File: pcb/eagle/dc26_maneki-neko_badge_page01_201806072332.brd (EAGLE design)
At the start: 100 x 80 mm, 49 parts, among them IC1 STM32F030C8T, T1 RK7002BMT116, U2 ESP01, X1 22-23-2021, X2 22-23-2031

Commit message: board outline in, some minor edits to schematic, board ready for component placement
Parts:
- removed LED1, LED2: WS2812B5050, adafruit_2015:WS2812B
- removed U$1, U$2: (no value), PSA08-11SRWA:PSA08-11SRWA
- removed U$5: PAM2301CAAB330, PAM2301CAAB120:SOT95P280X100-5N
- added C10: 1uF/16V/X7R, rcl:C0805
- added D1, D2: (no value), PSA08-11SRWA:PSA08-11SRWA
- added H3: TSW-102-07-G-D, con-samtec:TSW-102-XX-G-D
- added R26, R27, R28: 10k/5%, rcl:R0805
- added R29: NO POP, rcl:R0805
- added U3: ESP01, esp8266modules:ESP01
- C1: value SHORT -> 10uF/16V/X5R
- C3: value 10uF/16V/X5R -> SHORT
- R25: value 10k/5% -> 1k/5%
- U2: value ESP01 -> PAM2301CAAB330; device esp8266modules:ESP01 -> PAM2301CAAB120:SOT95P280X100-5N
- U5, U6: value (none) -> MIC2005A-1YM5-TR
- moved R3 129.2 mm to (38.5, 47.3), turned to 180 degrees
- moved C1 124.9 mm to (42.8, 43.6)
- moved C3 114.4 mm to (38.6, 39.1)
- moved C2 110.8 mm to (34.3, 44.8)
- moved R1 100.5 mm to (38.6, 41.2), turned to 180 degrees
- moved L1 95.7 mm to (35.7, 42.2), turned to 180 degrees
- moved U2 67.8 mm to (38.5, 44.1)
- moved R12 12.7 mm to (-105.4, -106.7)
- moved R14 12.7 mm to (-118.1, -106.7)
- moved R15 12.7 mm to (-105.4, -113.0)
- moved R17 12.7 mm to (-118.1, -113.0)
- moved R18 6.35 mm to (-111.8, -119.4)
- moved R19 6.35 mm to (-118.1, -119.4)
- renumbered IC1 to U1, U$13 to H1, U$3 to U6, U$4 to U5, U$6 to U4, X2 to H2
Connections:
- removed net VCC: C4.1, C5.1, C6.1, H1.1, R21.2, R22.2, U5.1, U6.1
- removed net VDDA: U1.9
- removed net VSSA: U1.8
- new net BOOT0: R28.2, R29.1, U1.44
- new net I2C1_SCL: H3.4, R26.1, U1.35
- new net I2C1_SDA: H3.3, R27.1, U1.36
- net !RESET: now also U1.7
- net 3V3: now also C10.1, C2.1, C4.1, C5.1, C6.1, H1.1, H3.1, R21.2, R22.2, R26.2, R27.2, R29.2, U1.9, U5.1, U6.1; no longer C1.1
- net ESP-CH_PD: now also U3.CH_PD; no longer U2.CH_PD
- net ESP-GPIO0: now also U3.GPIO0; no longer U2.GPIO0
- net ESP-GPIO2: now also U3.GPIO2; no longer U2.GPIO2
- net ESP-RST: now also U3.RST; no longer U2.RST
- net ESP-RXD: now also U3.RX; no longer U2.RX
- net ESP-TXD: now also U3.TX; no longer U2.TX
- net GND: now also C1.2, C10.2, H3.2, R28.1, U1.8, U2.2, U3.GND; no longer C3.2, LED1.3-GND, LED2.3-GND, U$5.2, U2.GND
- net LED-ANODE-LEFT: now also D1.11; no longer U$1.11
- net LED-ANODE-RIGHT: now also D2.11; no longer U$2.11
- net LED-SEG-A: now also D1.1, D2.1, R18.2; no longer R19.2, U$1.1, U$2.1
- net LED-SEG-B: now also D1.18, D2.18, R19.2; no longer R18.2, U$1.18, U$2.18
- net LED-SEG-C: now also D1.16, D2.16, R15.2; no longer R17.2, U$1.16, U$2.16
- net LED-SEG-D: now also D1.13, D2.13; no longer U$1.13, U$2.13
- net LED-SEG-DP: now also D1.12, D2.12; no longer U$1.12, U$2.12
- net LED-SEG-E: now also D1.10, D2.10, R17.2; no longer R15.2, U$1.10, U$2.10
- net LED-SEG-F: now also D1.9, D2.9, R12.2; no longer R14.2, U$1.9, U$2.9
- net LED-SEG-G: now also D1.8, D2.8; no longer U$1.8, U$2.8
- net LED-SEG-H: now also D1.4, D2.4, R14.2; no longer R12.2, U$1.4, U$2.4
- net LED-SEG-K: now also D1.3, D2.3; no longer U$1.3, U$2.3
- net LED-SEG-M: now also D1.2, D2.2; no longer U$1.2, U$2.2
- net LED-SEG-N: now also D1.17, D2.17; no longer U$1.17, U$2.17
- net LED-SEG-P: now also D1.15, D2.15; no longer U$1.15, U$2.15
- net LED-SEG-R: now also D1.14, D2.14; no longer U$1.14, U$2.14
- net LED-SEG-S: now also D1.6, D2.6; no longer U$1.6, U$2.6
- net LED-SEG-T: now also D1.7, D2.7; no longer U$1.7, U$2.7
- net LED-SEG-U: now also D1.5, D2.5; no longer U$1.5, U$2.5
- net N$1: now also U2.3; no longer U$5.3
- net N$2: now also U2.1; no longer U$5.1
- net N$3: now also C3.2, U2.5; no longer C1.2, U$5.5
- net PB0: now also R18.1; no longer R19.1
- net PB1: now also R19.1; no longer R18.1
- net PB2: now also R15.1; no longer R17.1
- net PB4: now also R17.1; no longer R15.1
- net PB5: now also R12.1; no longer R14.1
- net PB7: now also R14.1; no longer R12.1
- net VBAT: now also C1.1, U2.4; no longer C2.1, U$5.4
- net VDD: no longer LED1.1-VDD, LED2.1-VDD
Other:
- board size 100 x 80 mm -> 75.8 x 126.7 mm

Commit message: some component placement, eyes locked in
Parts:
- moved R29 433.2 mm to (61.4, 23.4), flipped to the bottom, turned to 90 degrees
- moved R28 424.5 mm to (55.2, 23.4), flipped to the bottom, turned to 90 degrees
- moved C10 415.8 mm to (49.1, 23.4), flipped to the bottom, turned to 90 degrees
- moved R27 407.1 mm to (42.9, 23.4), flipped to the bottom, turned to 90 degrees
- moved R26 398.4 mm to (36.8, 23.4), flipped to the bottom, turned to 90 degrees
- moved C9 389.8 mm to (30.6, 23.4), flipped to the bottom, turned to 90 degrees
- moved R22 386.3 mm to (55.4, 42.1), flipped to the bottom
- moved R20 385.1 mm to (52.5, 102.3), flipped to the bottom, turned to 270 degrees
- moved R21 384.0 mm to (55.4, 44.4), flipped to the bottom
- moved C8 382.6 mm to (59.6, 41.9), flipped to the bottom
- moved R25 381.1 mm to (24.5, 23.4), flipped to the bottom, turned to 90 degrees
- moved U4 380.3 mm to (60.2, 45.3), flipped to the bottom
- moved H2 378.0 mm to (54.5, 17.5), flipped to the bottom
- moved R23 378.0 mm to (46.4, 34.3), flipped to the bottom
- moved R24 378.0 mm to (46.4, 28.1), flipped to the bottom
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
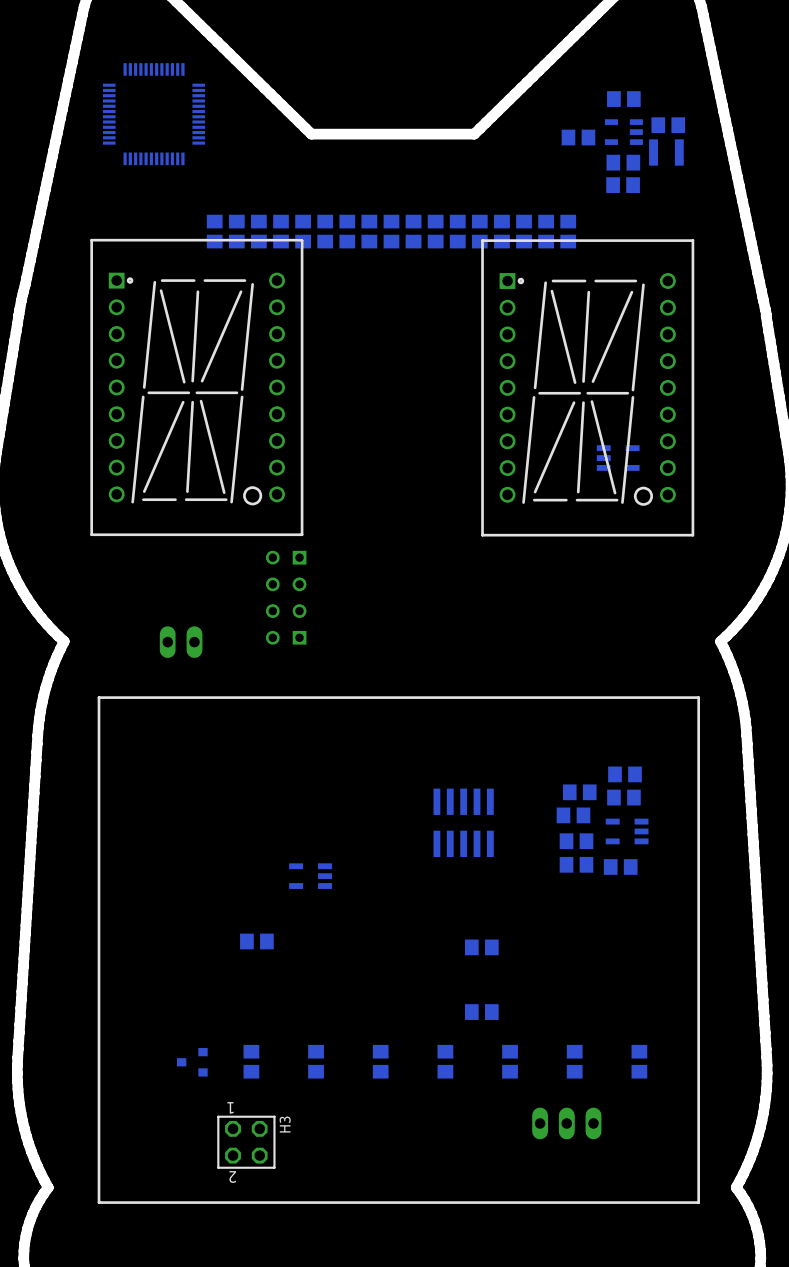
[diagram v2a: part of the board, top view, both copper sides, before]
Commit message: more layout. changed out connectors to support a clean 'art' (top) side. shooting for 2 layers, might need to be 4 to avoid a ton of routing time.
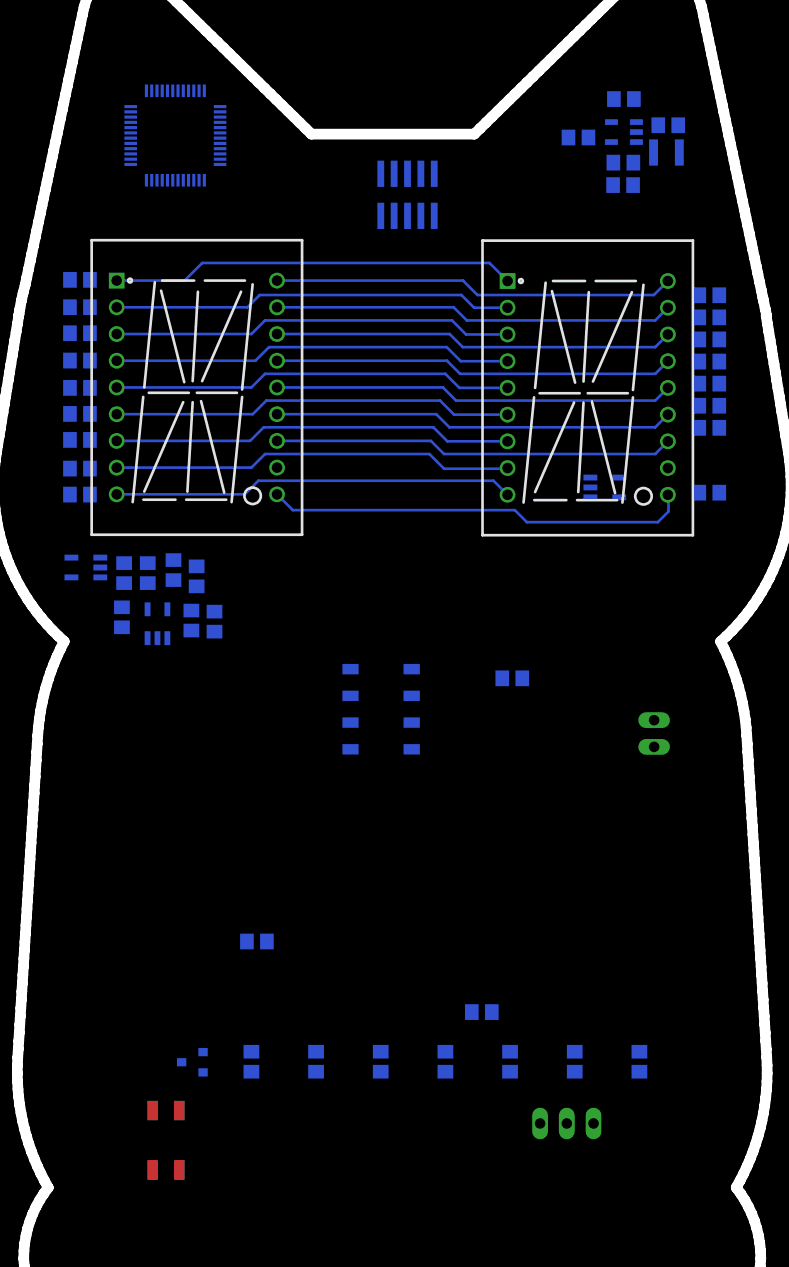
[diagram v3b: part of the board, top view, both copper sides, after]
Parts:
- H3: value TSW-102-07-G-D -> SHITTY-ADDON-HEADER-MASTER; device con-samtec:TSW-102-XX-G-D -> dc26-shitty-addon:2X2-0.1INCH-FEMALE-SMT
- U3: value ESP01 -> NPTC042KFMS-RC; device esp8266modules:ESP01 -> NPTC042KFMS-RC:NPTC042KFMS-RC
- moved H1 59.9 mm to (41.9, 103.8)
- moved C8 53.0 mm to (12.2, 65.6), turned to 90 degrees
- moved R22 51.2 mm to (12.4, 69.8), turned to 90 degrees
- moved U4 48.8 mm to (15.6, 65.0), turned to 90 degrees
- moved R21 48.1 mm to (14.6, 69.8), turned to 90 degrees
- moved X1 45.8 mm to (62.8, 54.6), turned to 90 degrees
- moved C7 44.6 mm to (17.1, 70.1), turned to 90 degrees
- moved C6 44.4 mm to (18.8, 65.3), turned to 90 degrees
- moved C5 41.8 mm to (19.3, 69.5), turned to 90 degrees
- moved C4 41.6 mm to (21.0, 65.2), turned to 90 degrees
- moved R12 38.8 mm to (8.19, 77.3), turned to 180 degrees
- moved U6 36.3 mm to (8.75, 70.4)
- moved R13 35.6 mm to (8.19, 79.8), turned to 180 degrees
- moved R5 32.2 mm to (8.19, 82.5), turned to 180 degrees
- moved R6 29.0 mm to (8.19, 85.0), turned to 180 degrees
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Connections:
- net 3V3: now also H3.VCC; no longer H3.1
- net ESP-CH_PD: now also U3.3; no longer U3.CH_PD
- net ESP-GPIO0: now also U3.6; no longer U3.GPIO0
- net ESP-GPIO2: now also U3.4; no longer U3.GPIO2
- net ESP-RST: now also U3.5; no longer U3.RST
- net ESP-RXD: now also U3.8; no longer U3.RX
- net ESP-TXD: now also U3.1; no longer U3.TX
- net ESP-VCC: now also U3.7
- net GND: now also H3.GND, U3.2; no longer H3.2, U3.GND
- net I2C1_SCL: now also H3.SCL; no longer H3.4
- net I2C1_SDA: now also H3.SDA; no longer H3.3
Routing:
- net LED-SEG-E: track 0.00 -> 40.3 mm
- net LED-SEG-A: track 0.00 -> 38.6 mm
- net LED-SEG-G: track 0.00 -> 38.3 mm
- net LED-SEG-B: track 0.00 -> 38.3 mm
- net LED-SEG-S: track 0.00 -> 38.2 mm
- net LED-SEG-H: track 0.00 -> 38.2 mm
- net LED-SEG-F: track 0.00 -> 38.2 mm
- net LED-SEG-U: track 0.00 -> 38.2 mm
- net LED-SEG-T: track 0.00 -> 38.2 mm
- net LED-SEG-K: track 0.00 -> 38.2 mm
- net LED-SEG-P: track 0.00 -> 38.2 mm
- net LED-SEG-N: track 0.00 -> 38.2 mm
- net LED-SEG-D: track 0.00 -> 38.2 mm
- net LED-SEG-C: track 0.00 -> 38.2 mm
- net LED-SEG-R: track 0.00 -> 38.2 mm
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
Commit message: completely regretting my decision to use eagle
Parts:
- added C11, C12: 1uF/16V/X7R, rcl:C0805
- moved R29 91.6 mm to (30.4, 109.6), turned to 180 degrees
- moved R28 87.6 mm to (30.3, 107.4), turned to 0 degrees
- moved C10 85.1 mm to (17.3, 102.4), turned to 180 degrees
- moved C2 75.4 mm to (15.3, 55.0), turned to 180 degrees
- moved R3 74.3 mm to (19.5, 52.5), turned to 0 degrees
- moved L1 69.6 mm to (16.7, 57.6), turned to 0 degrees
- moved U2 69.1 mm to (19.5, 55.6), turned to 180 degrees
- moved H2 67.1 mm to (10.8, 68.4), turned to 270 degrees
- moved R1 64.5 mm to (19.5, 58.5), turned to 0 degrees
- moved C1 63.6 mm to (23.8, 56.1), turned to 180 degrees
- moved C3 61.2 mm to (19.6, 60.7), turned to 180 degrees
- moved R27 46.4 mm to (9.27, 55.3)
- moved T1 45.6 mm to (16.0, 68.8)
- moved C6 45.4 mm to (43.2, 103.6)
- moved C9 44.3 mm to (10.8, 63.0), turned to 0 degrees
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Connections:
- removed net VDD: U1.1, U1.24, U1.48
- removed net VSS: U1.23, U1.47
- net 3V3: now also C11.1, C12.1, U1.1, U1.24, U1.48
- net GND: now also C11.2, C12.2, U1.23, U1.47
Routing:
- net PB0: track 0.00 -> 14.3 mm
- net N$3: track 0.00 -> 9.18 mm
- net 3V3: track 0.00 -> 8.56 mm
- net VBAT: track 0.00 -> 7.03 mm
- net LED-ANODE-LEFT: track 0.00 -> 6.72 mm
- net LED-ANODE-RIGHT: track 0.00 -> 5.78 mm
- net N$1: track 0.00 -> 2.53 mm
- net N$2: track 0.00 -> 2.30 mm

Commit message: mini commit before taking a shower and letting autorouter mess around
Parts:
- removed X1: 22-23-2021, con-molex:22-23-2021
- added U$1: BATTPADS-SMT, battery_pads:BATTPADS-SMT
- moved R24 22.0 mm to (27.8, 62.0), turned to 90 degrees
- moved R22 20.8 mm to (29.9, 62.0), turned to 270 degrees
- moved R23 16.7 mm to (32.1, 62.0), turned to 90 degrees
- moved R21 15.2 mm to (34.2, 62.0), turned to 270 degrees
- moved U3 2.13 mm to (39.9, 66.5)
- moved C7 2.13 mm to (26.8, 67.5)
- moved U4 2.13 mm to (23.3, 67.6)
- moved C8 2.13 mm to (23.2, 64.4)
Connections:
- net GND: now also U$1.2; no longer X1.2
- net VBAT: now also U$1.1; no longer X1.1
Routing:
- net VBAT: track 7.03 -> 22.0 mm

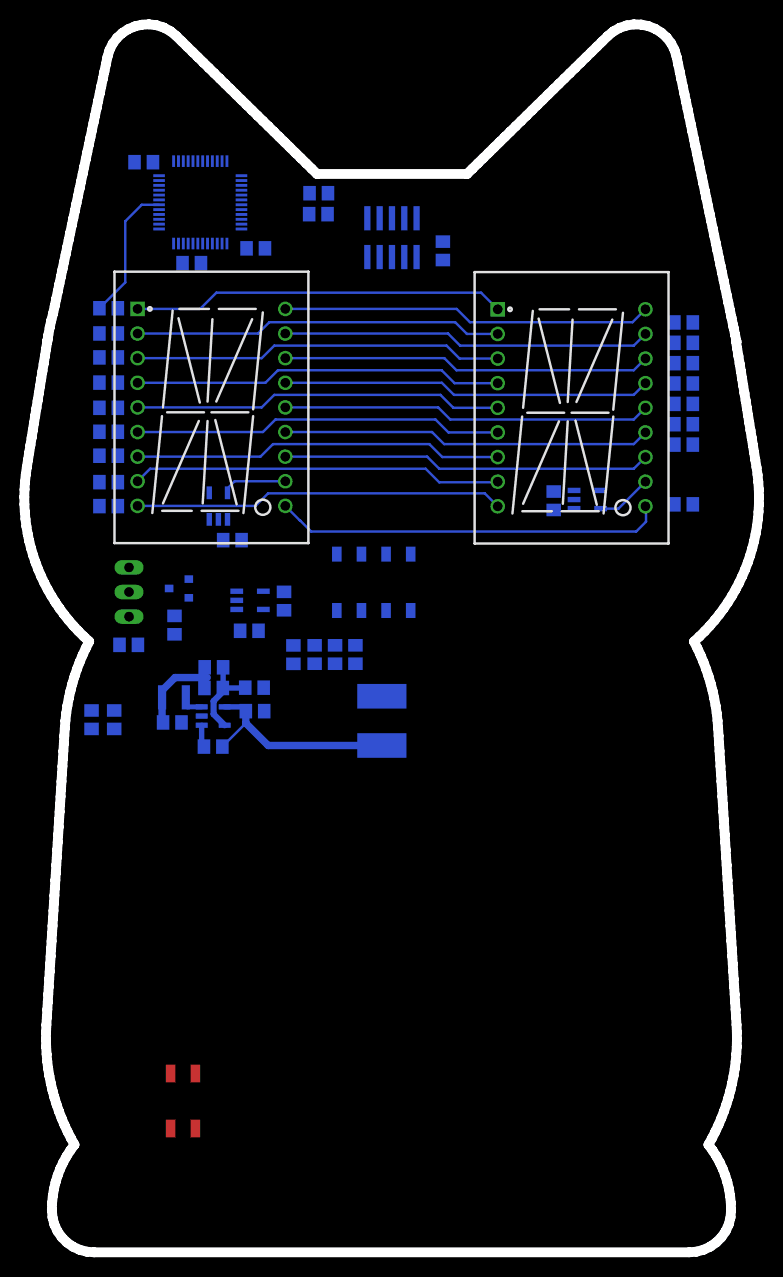
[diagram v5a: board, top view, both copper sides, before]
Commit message: re-orging traces to eyes for clean routing, done routing left eye
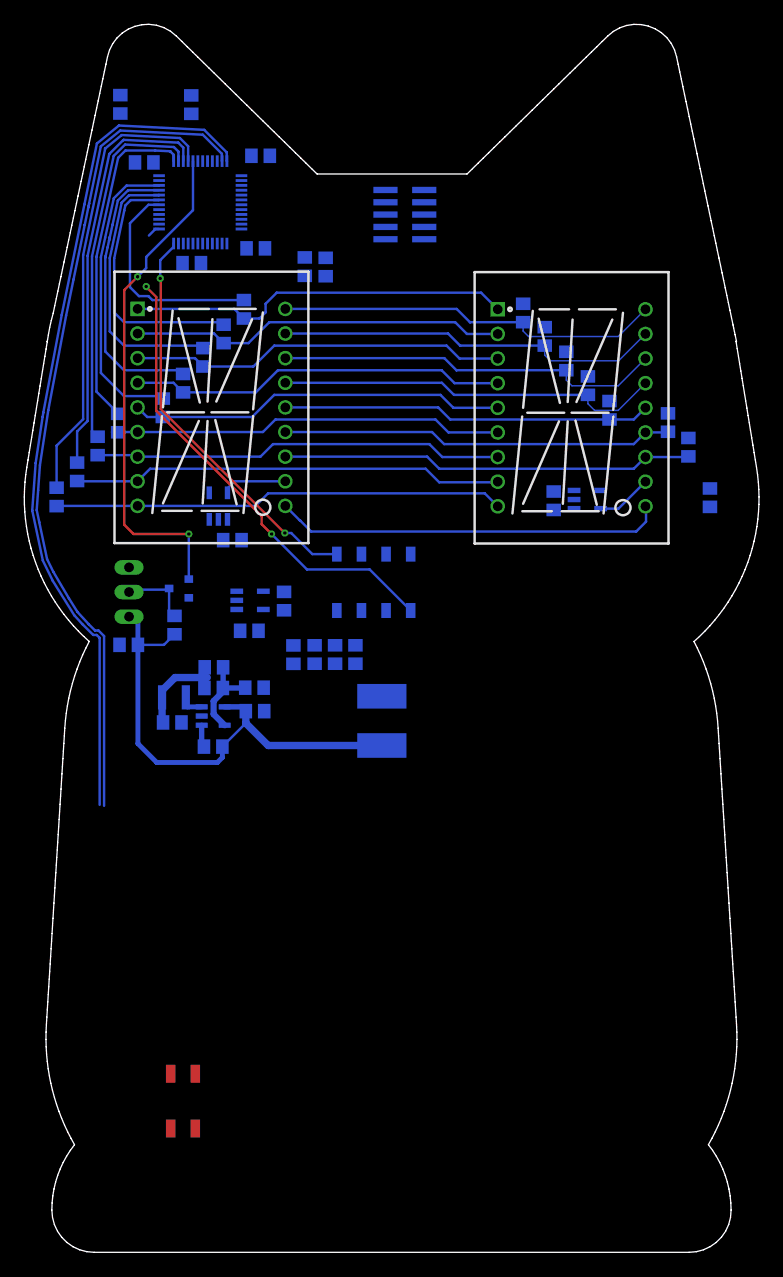
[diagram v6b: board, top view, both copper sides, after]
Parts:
- moved R27 63.9 mm to (17.2, 118.7)
- moved R26 60.7 mm to (24.4, 113.4), turned to 180 degrees
- moved C6 36.5 mm to (9.91, 118.7), turned to 270 degrees
- moved R19 16.6 mm to (51.5, 97.2), turned to 270 degrees
- moved R9 14.3 mm to (53.7, 94.8), turned to 270 degrees
- moved R18 14.0 mm to (22.7, 97.6), turned to 270 degrees
- moved R15 12.1 mm to (55.9, 92.3), turned to 270 degrees
- moved R10 11.9 mm to (20.6, 95.1), turned to 270 degrees
- moved R8 9.87 mm to (58.1, 89.7), turned to 270 degrees
- moved R11 9.77 mm to (18.5, 92.6), turned to 270 degrees
- moved R14 7.68 mm to (16.4, 90.0), turned to 270 degrees
- moved R7 7.67 mm to (60.4, 87.2), turned to 270 degrees
- moved R29 7.65 mm to (31.1, 102.0), turned to 270 degrees
- moved H1 6.96 mm to (41.3, 109.9), turned to 270 degrees
- moved R28 5.59 mm to (28.9, 102.0), turned to 90 degrees
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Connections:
- new net N$: R7.1
- new net N$14: R17.1
- new net N$15: R16.1
- new net N$19: R9.1
- new net N$8: R8.1
- net PB1: now also R10.1
- net PB10: now also R14.1; no longer R9.1
- net PB11: now also R4.1; no longer R8.1
- net PB12: now also R6.1; no longer R7.1
- net PB13: now also R5.1; no longer R6.1
- net PB14: now also R13.1; no longer R5.1
- net PB15: now also R12.1; no longer R4.1
- net PB2: now also R11.1
- net PB3: no longer R16.1
- net PB4: no longer R17.1
- net PB5: no longer R12.1
- net PB6: no longer R13.1
- net PB7: no longer R14.1
- net PB8: no longer R11.1
- net PB9: no longer R10.1
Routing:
- net I2C1_SDA: track 0.00 -> 87.0 mm
- net I2C1_SCL: track 0.00 -> 85.6 mm
- net SERVO-PWM: track 0.00 -> 52.2 mm, vias 0 -> 2
- net ESP-TXD: track 0.00 -> 49.8 mm, vias 0 -> 2
- net PB15: track 0.00 -> 47.4 mm
- net PB14: track 0.00 -> 42.4 mm
- net ESP-RXD: track 0.00 -> 42.0 mm, vias 0 -> 2
- net PB13: track 0.00 -> 37.8 mm
- net PB12: track 0.00 -> 34.4 mm
- net PB11: track 0.00 -> 30.9 mm
- net PB10: track 0.00 -> 29.4 mm
- net VBAT: track 22.0 -> 51.1 mm
- net PB2: track 0.00 -> 28.0 mm
- net PB1: track 0.00 -> 26.7 mm
- net PB0: track 14.3 -> 22.7 mm
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
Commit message: all led and high(er) speed signals routed... phewf
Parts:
- moved H1 23.8 mm to (63.4, 118.7)
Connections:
- removed net N$: R7.1
- removed net N$14: R17.1
- removed net N$15: R16.1
- removed net N$19: R9.1
- removed net N$8: R8.1
- net PB1: no longer R19.1
- net PB2: no longer R15.1
- net PB3: now also R17.1
- net PB4: now also R16.1
- net PB5: now also R7.1
- net PB6: now also R8.1
- net PB7: now also R15.1
- net PB8: now also R9.1
- net PB9: now also R19.1
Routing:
- net PA15: track 0.00 -> 105.4 mm, vias 0 -> 2
- net PB3: track 0.00 -> 75.3 mm
- net PB5: track 0.00 -> 68.9 mm
- net PB6: track 0.00 -> 67.6 mm
- net PB4: track 0.00 -> 67.6 mm
- net PB7: track 0.00 -> 67.3 mm
- net PB8: track 0.00 -> 39.5 mm
- net PB9: track 0.00 -> 35.7 mm
- net ESP-TXD: track 49.8 -> 57.3 mm
- net LED-SEG-E: track 40.3 -> 46.9 mm
- net PB0: track 22.7 -> 23.5 mm

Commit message: pcb traces routed, just need to finish off GND and 3V3 rails
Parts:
- moved C6 51.5 mm to (61.4, 121.2), turned to 0 degrees
- moved T1 11.4 mm to (5.26, 72.7), turned to 0 degrees
- moved R25 9.91 mm to (6.35, 68.8)
- moved C8 3.36 mm to (20.8, 66.7), turned to 0 degrees
- moved C7 2.03 mm to (28.8, 67.5)
- moved U4 2.03 mm to (25.3, 67.6)
- moved C10 0.47 mm to (17.1, 101.9)
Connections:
- net ESP-CH_PD: now also U1.10
- net ESP-RST: now also U1.11
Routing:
- net ESP-GPIO0: track 0.00 -> 88.6 mm, vias 0 -> 2
- net ESP-GPIO2: track 0.00 -> 83.1 mm, vias 0 -> 2
- net ESP-CH_PD: track 0.00 -> 80.8 mm, vias 0 -> 3
- net EYE-RIGHT-EN: track 0.00 -> 72.3 mm, vias 0 -> 2
- net ESP-EN: track 0.00 -> 71.9 mm, vias 0 -> 2
- net RIGHT-EYE-!FAULT: track 0.00 -> 66.7 mm, vias 0 -> 2
- net ESP-!FAULT: track 0.00 -> 55.1 mm, vias 0 -> 2
- net !RESET: track 0.00 -> 51.9 mm, vias 0 -> 2
- net ESP-RST: track 0.00 -> 48.1 mm, vias 0 -> 2
- net SWDIO: track 0.00 -> 46.8 mm, vias 0 -> 2
- net EYE-LEFT-EN: track 0.00 -> 44.8 mm, vias 0 -> 2
- net LEFT-EYE-!FAULT: track 0.00 -> 43.8 mm, vias 0 -> 2
- net SWCLK: track 0.00 -> 41.7 mm
- net BOOT0: track 0.00 -> 14.7 mm, vias 0 -> 2
- net ESP-TXD: track 57.3 -> 64.6 mm
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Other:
- outline, holes or cut-outs redrawn
- board text added: "BATT+"
- board text added: "BATT-"
